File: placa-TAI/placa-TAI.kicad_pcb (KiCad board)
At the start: 2 copper layers, 18 parts, among them SW1 SW_Push, SW2 SW_Push, U1 ESP-WROOM-02

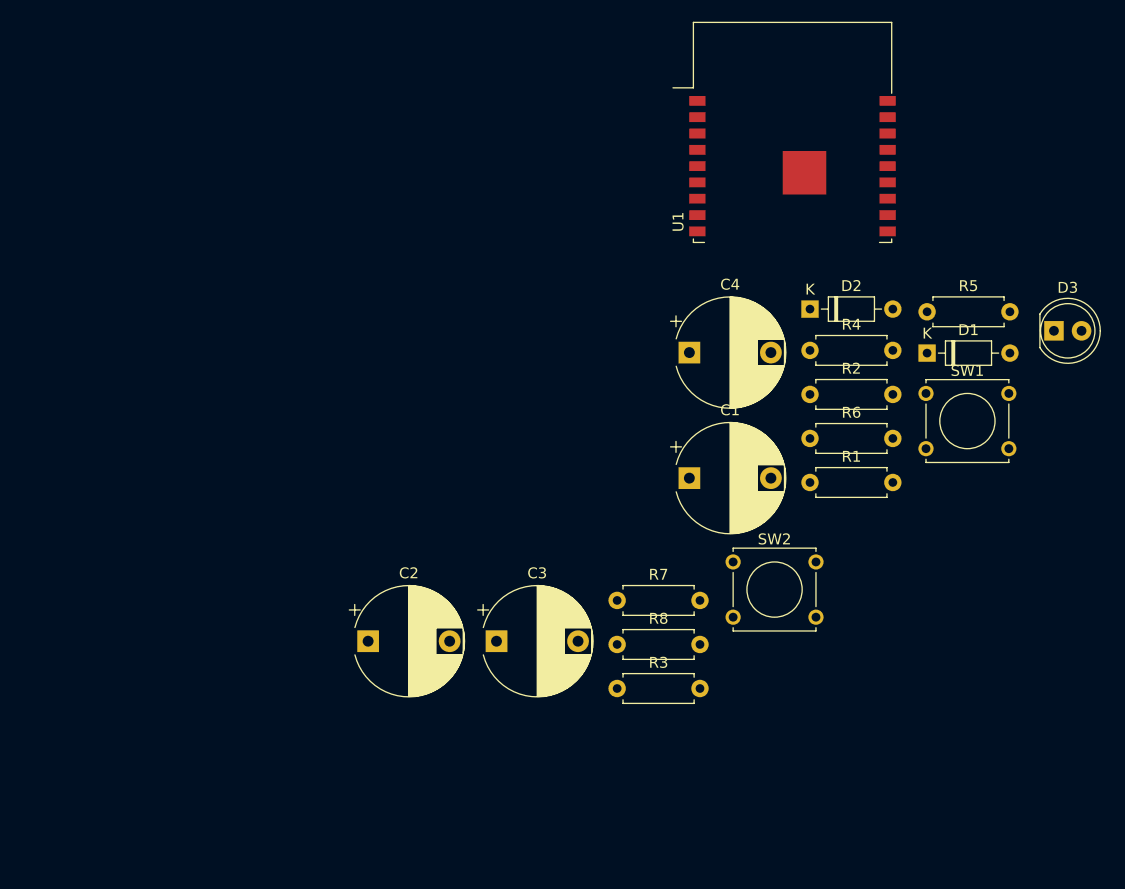
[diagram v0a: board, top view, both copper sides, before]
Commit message: Add files via upload
Alterei o esp82 para o esp32
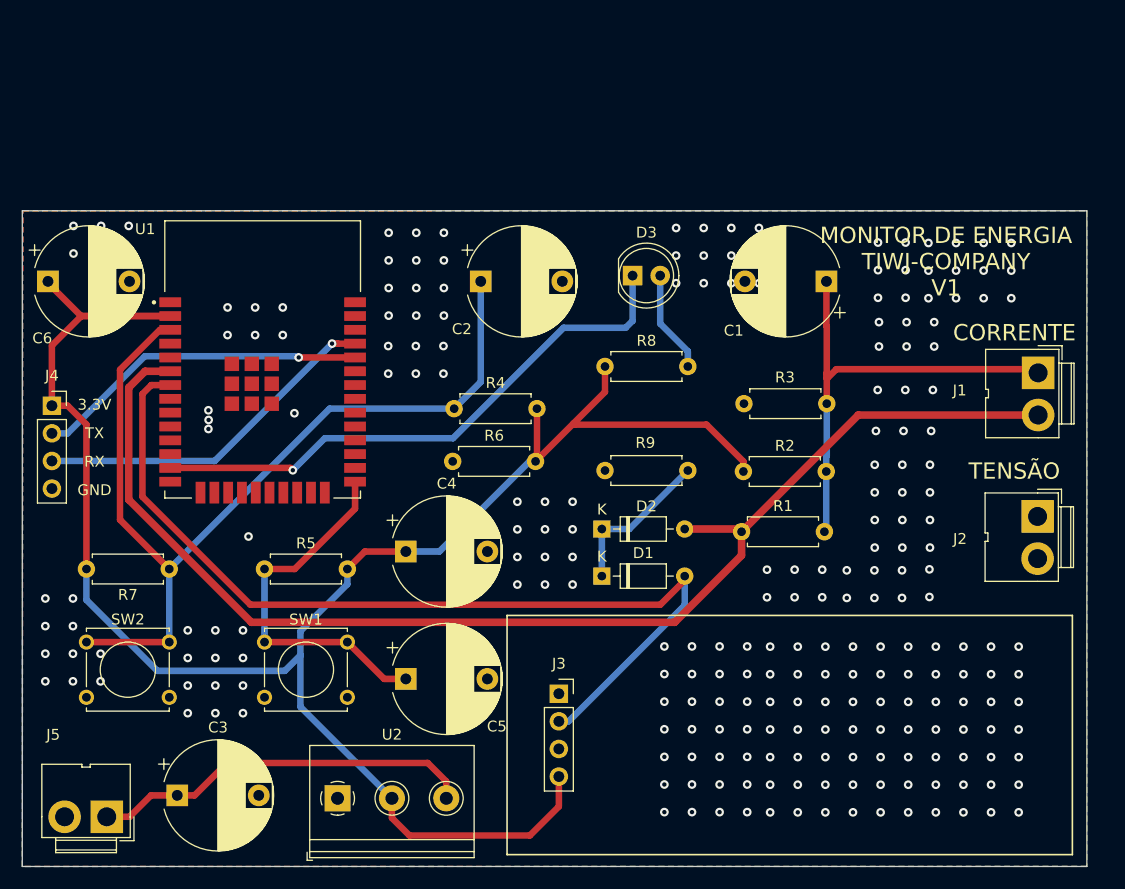
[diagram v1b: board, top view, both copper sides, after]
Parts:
- added C5: 100n, Capacitor_THT:CP_Radial_D10.0mm_P7.50mm, F.Cu at (126.4, 103.8)
- added C6: 100n, Capacitor_THT:CP_Radial_D10.0mm_P7.50mm, F.Cu at (93.5, 67.2)
- added J1: Screw_Terminal_01x02, Connector:JWT_A3963_1x02_P3.96mm_Vertical, F.Cu at (184.6, 75.6)
- added J2: Screw_Terminal_01x02, Connector:JWT_A3963_1x02_P3.96mm_Vertical, F.Cu at (184.5, 88.8)
- added J3: Conn_01x04_Female, Connector_PinSocket_2.54mm:PinSocket_1x04_P2.54mm_Vertical, F.Cu at (140.5, 105.1)
- added J4: Conn_01x04_Male, Connector_PinSocket_2.54mm:PinSocket_1x04_P2.54mm_Vertical, F.Cu at (93.9, 78.6)
- added J5: Screw_Terminal_01x02, Connector:JWT_A3963_1x02_P3.96mm_Vertical, F.Cu at (98.9, 116.4)
- added R9: 10k, Resistor_THT:R_Axial_DIN0207_L6.3mm_D2.5mm_P7.62mm_Horizontal, F.Cu at (152.4, 84.6)
- added U2: LM1117-3.3, TerminalBlock_Philmore:TerminalBlock_Philmore_TB133_1x03_P5.00mm_Horizontal, F.Cu at (120.2, 114.7)
- R8: value 475k -> 470
- U1: value ESP-WROOM-02 -> ESP32-WROOM-32; footprint RF_Module:ESP-WROOM-02 -> esp32:MODULE_ESP32-WROOM-32
- moved R5 65.4 mm to (113.4, 93.6)
- moved SW1 65.0 mm to (113.4, 100.4)
- moved SW2 59.9 mm to (97.0, 100.4)
- moved U1 51.9 mm to (113.3, 74.4)
- moved R7 41.3 mm to (104.7, 93.6), turned to 180 degrees
- moved D3 39.1 mm to (147.3, 66.7)
- moved D1 36.3 mm to (144.5, 94.3)
- moved C2 34.7 mm to (133.3, 67.2)
- moved R4 33.2 mm to (130.9, 78.9)
- moved R6 32.9 mm to (130.7, 83.7)
- moved C3 32.6 mm to (105.4, 114.5)
- moved R3 32.5 mm to (165.2, 78.4), turned to 180 degrees
- moved C4 31.9 mm to (126.4, 92.0)
- moved D2 27.9 mm to (144.5, 90.0)
- moved R8 25.6 mm to (144.8, 75.0)
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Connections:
- C2 pad 1: 3.3V -> FSH
- R2 pad 1: CORRENTE_CONTROL -> 3.3V
- R4 pad 1: Net-(R4-Pad1) -> FSH
- U1 pad 1: 3.3V -> GND
- U1 pad 10: Net-(R6-Pad1) -> unconnected-(U1-Pad10)
- U1 pad 11: TX -> unconnected-(U1-Pad11)
- U1 pad 12: RX -> unconnected-(U1-Pad12)
- U1 pad 13: GND -> LED
- U1 pad 15: RST -> GND
- U1 pad 16: ADCX -> unconnected-(U1-Pad16)
- U1 pad 17: RST -> unconnected-(U1-Pad17)
- U1 pad 18: GND -> unconnected-(U1-Pad18)
- U1 pad 19: GND -> unconnected-(U1-Pad19)
- U1 pad 2: Net-(R4-Pad1) -> 3.3V
- U1 pad 3: CORRENTE_CONTROL -> FSH
- U1 pad 5: TENSAO_CONTROL -> unconnected-(U1-Pad5)
- U1 pad 6: LED -> ADC0
- U1 pad 7: unconnected-(U1-Pad7) -> ADC1
- U1 pad 8: FSH -> unconnected-(U1-Pad8)
- U1 pad 9: GND -> unconnected-(U1-Pad9)
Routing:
- net 3.3V: track 0.00 -> 177.0 mm
- net ADC0: track 0.00 -> 117.6 mm
- net ADC1: track 0.00 -> 86.3 mm
- net FSH: track 0.00 -> 85.7 mm
- net LED: track 0.00 -> 52.5 mm, vias 0 -> 1
- net Net-(C1-Pad1): track 0.00 -> 43.6 mm
- net 5V: track 0.00 -> 35.5 mm
- net RST: track 0.00 -> 33.3 mm
- net RX: track 0.00 -> 32.4 mm, vias 0 -> 1
- net TX: track 0.00 -> 30.9 mm, vias 0 -> 1
- net ADCX: track 0.00 -> 14.5 mm
- net Net-(D3-Pad2): track 0.00 -> 9.41 mm
- net GND: vias 0 -> 235
- added copper zone on B.Cu, net GND
- added copper zone on F.Cu, net GND
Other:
- board outline added: 97.9 x 60.3 mm
- board text added: "3.3V"
- board text added: "CORRENTE"
- board text added: "GND"
- board text added: "MONITOR DE ENERGIA TIWJ-COMPANY V1"
- board text added: "RX"
- board text added: "TENSÃO"
- board text added: "TX"
